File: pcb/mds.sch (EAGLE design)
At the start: 51 parts, among them IC1 MAX1555, Q1 CSTCR6M00G53Z, U2 ISD1900ISD1932, U5 ATMEGA328

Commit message: Code
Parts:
- R6: value (none) -> 56k
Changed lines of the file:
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@@
 <part name="SP-" library="wirepad" deviceset="2,15/1,0" device=""/>
 <part name="R8" library="rcl" deviceset="R-EU_" device="M0805" value="10k"/>
-<part name="R6" library="rcl" deviceset="R-EU_" device="M0805"/>
+<part name="R6" library="rcl" deviceset="R-EU_" device="M0805" value="56k"/>
 <part name="GND2" library="SparkFun" deviceset="GND" device=""/>
 <part name="R3" library="rcl" deviceset="R-EU_" device="M0805" value="4.7k"/>

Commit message: Code !
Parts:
- removed BTN: Button, SparkFun:TAC_SWITCHSMD
- removed MOT+, MOT-: (no value), wirepad:2,15/1,0
- removed RESET: Reset, SparkFun:TAC_SWITCHSMD
- added ADC1, VIB+, VIB-: (no value), wirepad:1,6/0,8
- added C13: 100nf, rcl:C-EUC0805
- added R9: 4.7k, rcl:R-EU_M0805
- added RST+, RST-: WIREPAD1,6/0,8, wirepad:WIREPAD1,6/0,8
- ADC0, LIPO+, LIPO-, MIC+, MIC-, PWR+, PWR-, SP+, SP-: device wirepad:2,15/1,0 -> wirepad:1,6/0,8
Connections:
- new net ADC1: ADC1.P, C13.1, U5.ADC7
- net ADC0: now also U5.ADC6; no longer BTN.1, BTN.2, U5.PC0(ADC0)
- net CHG: now also R9.1
- net GND: now also C13.2, RST-.P; no longer BTN.3, BTN.4, RESET.1, RESET.2
- net M3: now also U5.PC0(ADC0); no longer U5.ADC6
- net M4: no longer U5.ADC7
- net N$7: now also VIB-.P; no longer MOT-.P
- net RST: now also RST+.P; no longer RESET.3, RESET.4
- net VCC: now also R9.2, VIB+.P; no longer MOT+.P
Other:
- moved on the sheet: C10, C18

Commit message: Code + Cad
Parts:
- removed Q1: CSTCR6M00G53Z, murata-filter:CSTCR6M00G53Z
- added C14, C21, C22: 100nf, rcl:C-EUC0805
- added LED1: (no value), led:LEDCHIP-LED0805
- added R10: 4.7k, rcl:R-EU_M0805
- added U3: SF-BLUEGIGA_BLE112-A-VISUAL, ble112:SF-BLUEGIGA_BLE112-A-VISUAL
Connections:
- removed net N$9: Q1.3, U5.PB7(XTAL2/TOSC2)
- new net ??: U5.PB7(XTAL2/TOSC2)
- new net LEDB: R10.2, U3.P0_0
- new net RX: U3.P0_5
- new net TX: U3.P0_4
- net GND: now also C14.1, C21.1, C22.1, LED1.C, U3.GND, U3.GND@2, U3.GND@3, U3.GND@4; no longer Q1.2
- net M4: now also U5.PC1(ADC1)
- net N$10: now also LED1.A, R10.1; no longer Q1.1, U5.PB6(XTAL1/TOSC1)
- net VCC: now also C14.2, C21.2, C22.2, U3.AVDD, U3.AVDD@2, U3.DVDD, U3.VDD_USB
- net VIBRATOR: now also U5.PB6(XTAL1/TOSC1); no longer U5.PC1(ADC1)
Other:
- note added: "Bluetooth"
- moved on the sheet: C1, C19, C2, C20, C3, C4, C5, C6, C7, C8, MIC+, MIC-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

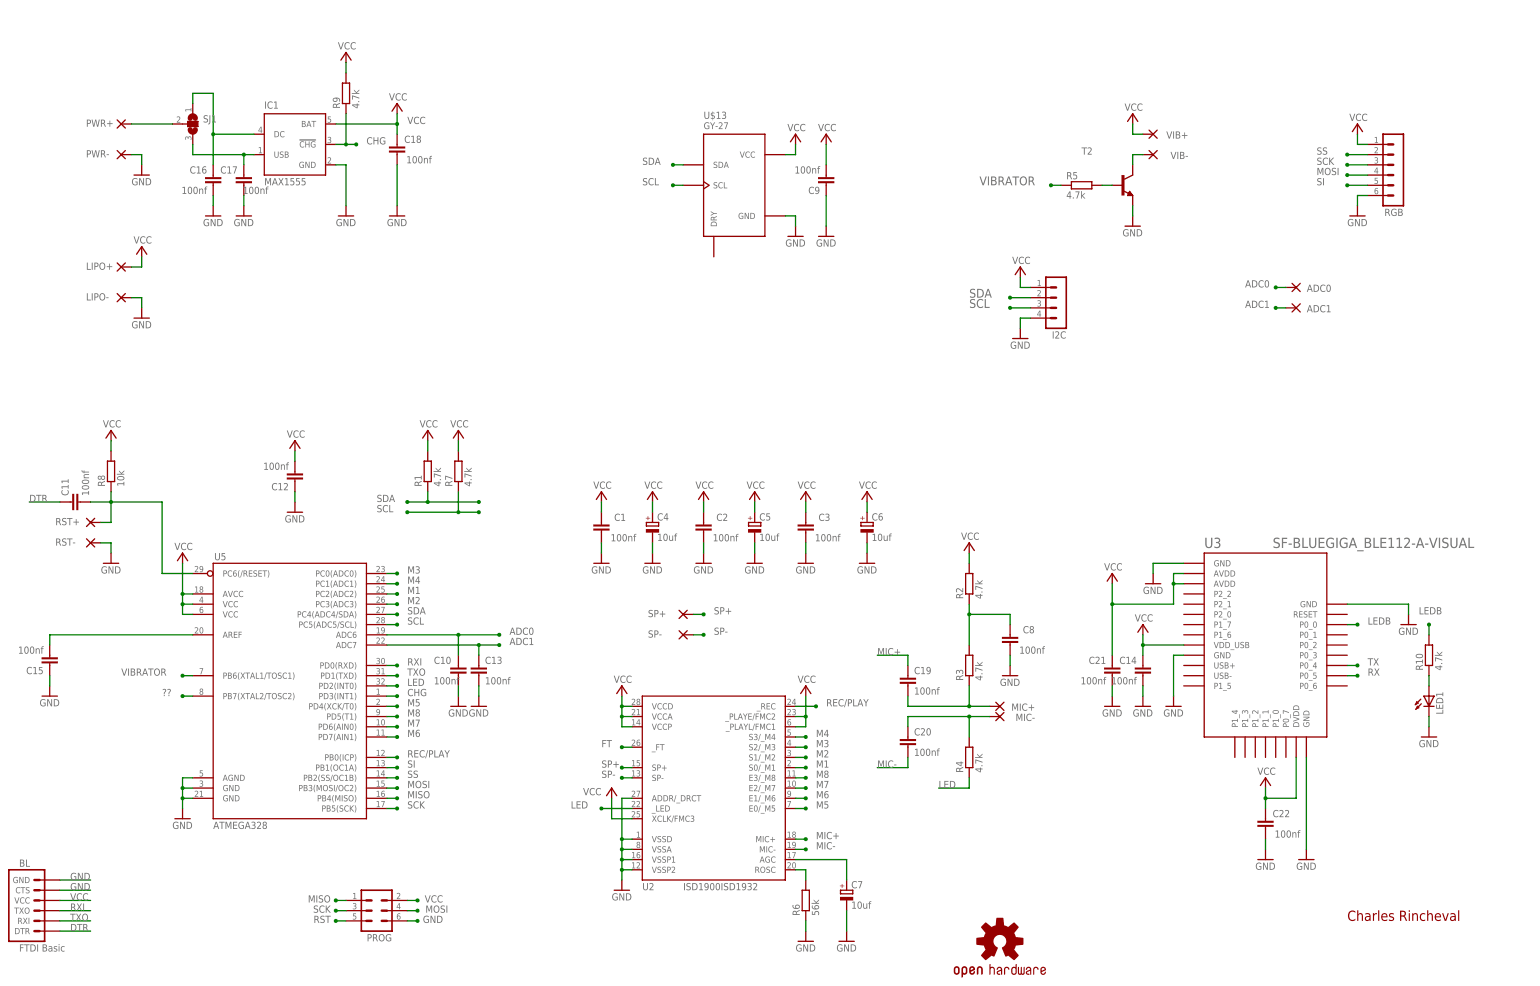
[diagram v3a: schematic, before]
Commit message: PCB : Bluetooth module + enhancement
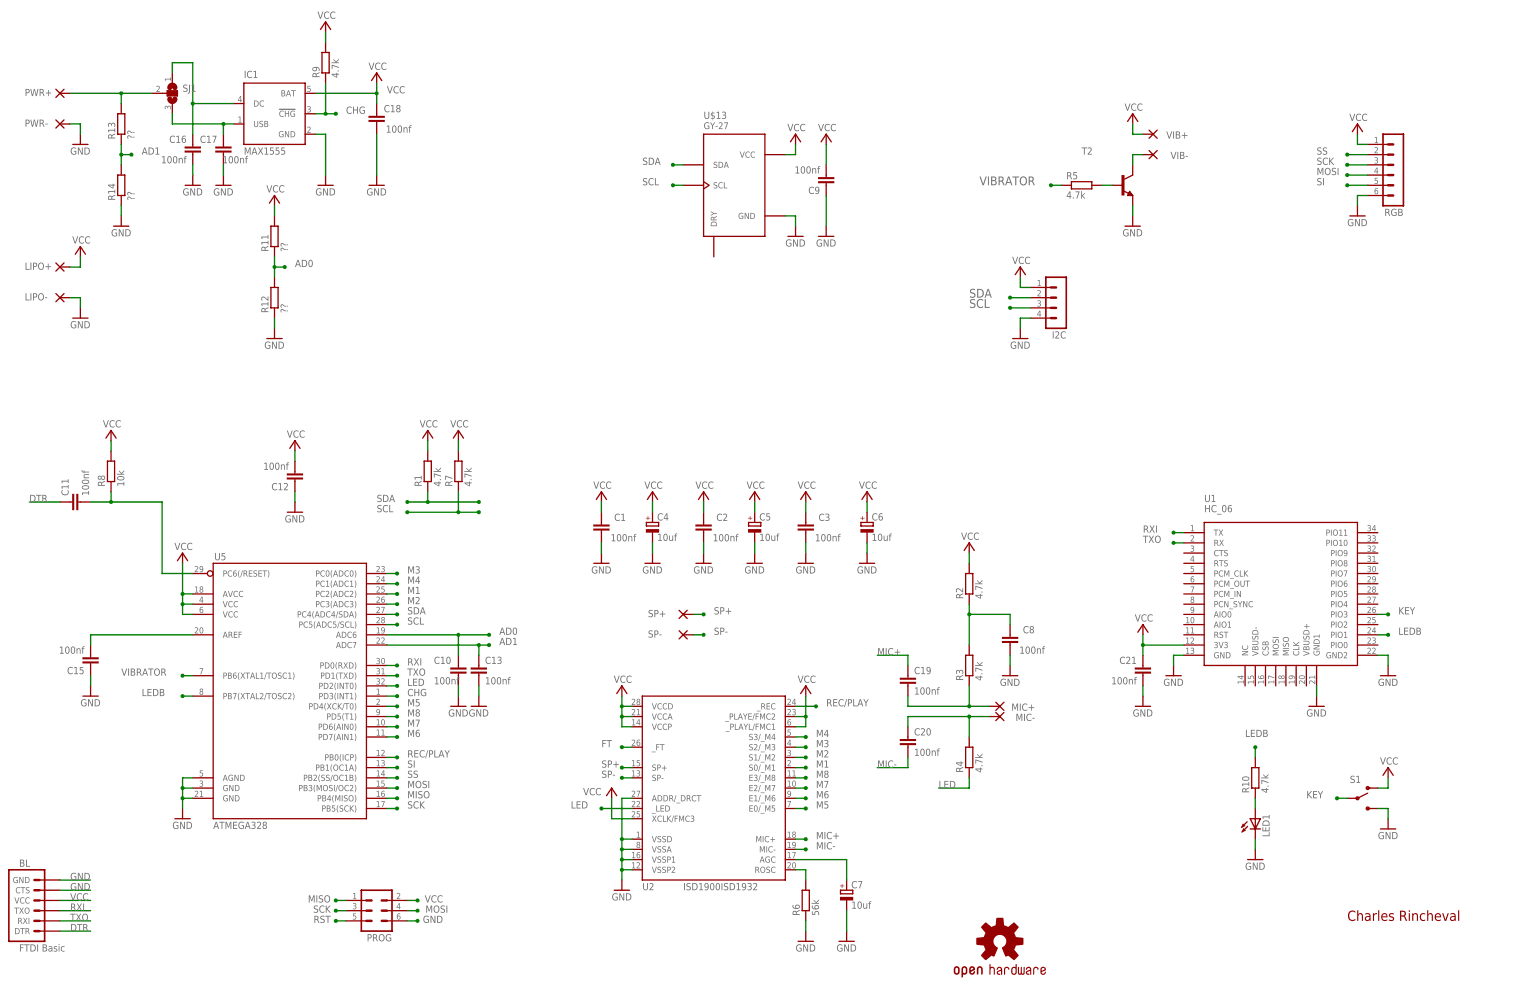
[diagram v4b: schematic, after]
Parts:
- removed ADC0, ADC1: (no value), wirepad:1,6/0,8
- removed C14, C22: 100nf, rcl:C-EUC0805
- removed RST+, RST-: WIREPAD1,6/0,8, wirepad:WIREPAD1,6/0,8
- removed U3: SF-BLUEGIGA_BLE112-A-VISUAL, ble112:SF-BLUEGIGA_BLE112-A-VISUAL
- added R11, R12, R13, R14: ??, rcl:R-EU_M0805
- added S1: (no value), SparkFun-Electromechanical:SWITCH-SPDTSMD2
- added U1: HC_06, Bluetooth HC-05:HC_05
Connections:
- removed net ??: U5.PB7(XTAL2/TOSC2)
- removed net ADC0: ADC0.P, C10.1, U5.ADC6
- removed net ADC1: ADC1.P, C13.1, U5.ADC7
- removed net RX: U3.P0_5
- removed net TX: U3.P0_4
- new net AD0: C10.1, R11.1, R12.2, U5.ADC6
- new net AD1: C13.1, R13.1, R14.2, U5.ADC7
- new net KEY: S1.P, U1.PIO3
- net GND: now also R12.1, R14.1, S1.S, U1.GND, U1.GND1, U1.GND2; no longer C14.1, C22.1, RST-.P, U3.GND, U3.GND@2, U3.GND@3, U3.GND@4
- net LEDB: now also U1.PIO1, U5.PB7(XTAL2/TOSC2); no longer U3.P0_0
- net N$8: now also R13.2
- net RST: no longer RST+.P
- net RXI: now also U1.TX
- net TXO: now also U1.RX
- net VCC: now also R11.2, S1.O, U1.3V3; no longer C14.2, C22.2, U3.AVDD, U3.AVDD@2, U3.DVDD, U3.VDD_USB
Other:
- moved on the sheet: C15, C16, C17, C18, C21, IC1, LED1, LIPO+, LIPO-, PWR+, PWR-, R10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

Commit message: PCB 0.8.0
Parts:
- removed LED1: (no value), led:LEDCHIP-LED0805
- added LED: (no value), led:LEDCHIP-LED0805
- added SJ2, SJ3: (no value), jumper:SJ2W
- BLUETOOTH: value HC_06 -> HC_0x
- renumbered U1 to BLUETOOTH
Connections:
- removed net KEY: BLUETOOTH.PIO3, S1.P
- new net HC05_KEY: BLUETOOTH.PIO11, SJ2.3
- new net HC05_LED: BLUETOOTH.PIO9, SJ3.3
- new net HC06_KEY: BLUETOOTH.PIO3, SJ2.1
- new net HC06_LED: BLUETOOTH.PIO1, SJ3.1
- new net N$4: S1.P, SJ2.2
- net GND: now also LED.C; no longer LED1.C
- net LEDB: now also SJ3.2; no longer BLUETOOTH.PIO1
- net N$10: now also LED.A; no longer LED1.A
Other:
- moved on the sheet: R10, S1
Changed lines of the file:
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@@
 <part name="C21" library="rcl" deviceset="C-EU" device="C0805" value="100nf"/>
 <part name="R10" library="rcl" deviceset="R-EU_" device="M0805" value="4.7k"/>
-<part name="LED1" library="led" deviceset="LED" device="CHIP-LED0805"/>
+<part name="LED" library="led" deviceset="LED" device="CHIP-LED0805"/>
 <part name="GND35" library="SparkFun" deviceset="GND" device=""/>
-<part name="U1" library="Bluetooth HC-05" deviceset="HC_05" device="" value="HC_06"/>
+<part name="BLUETOOTH" library="Bluetooth HC-05" deviceset="HC_05" device="" value="HC_0x"/>
 <part name="GND30" library="SparkFun" deviceset="GND" device=""/>
 <part name="GND31" library="SparkFun" deviceset="GND" device=""/>
@@
 <part name="R14" library="rcl" deviceset="R-EU_" device="M0805" value="??"/>
 <part name="GND33" library="SparkFun" deviceset="GND" device=""/>
+<part name="SJ2" library="jumper" deviceset="SJ2W" device=""/>
+<part name="SJ3" library="jumper" deviceset="SJ2W" device=""/>
 </parts>
 <sheets>
@@
 <attribute name="VALUE" x="295.656" y="80.899" size="1.778" layer="96" rot="R180"/>
 </instance>
-<instance part="R10" gate="G$1" x="325.12" y="55.88" rot="R90"/>
-<instance part="LED1" gate="G$1" x="325.12" y="45.72"/>
-<instance part="GND35" gate="1" x="325.12" y="35.56"/>
-<instance part="U1" gate="G$1" x="330.2" y="101.6"/>
+<instance part="R10" gate="G$1" x="297.18" y="55.88" rot="R90"/>
+<instance part="LED" gate="G$1" x="297.18" y="45.72"/>
+<instance part="GND35" gate="1" x="297.18" y="35.56"/>
+<instance part="BLUETOOTH" gate="G$1" x="330.2" y="101.6"/>
 <instance part="GND30" gate="1" x="304.8" y="81.28"/>
 <instance part="GND31" gate="1" x="340.36" y="73.66"/>
-<instance part="S1" gate="1" x="350.52" y="50.8" smashed="yes">
-<attribute name="NAME" x="348.615" y="54.61" size="1.778" layer="95"/>
-<attribute name="VALUE" x="347.98" y="54.61" size="1.778" layer="96"/>
-</instance>
-<instance part="GND27" gate="1" x="358.14" y="43.18"/>
-<instance part="P+25" gate="VCC" x="358.14" y="58.42" smashed="yes">
-<attribute name="VALUE" x="360.68" y="60.96" size="1.778" layer="96" rot="R180"/>
+<instance part="S1" gate="1" x="330.2" y="50.8" smashed="yes">
+<attribute name="NAME" x="328.295" y="54.61" size="1.778" layer="95"/>
+<attribute name="VALUE" x="327.66" y="54.61" size="1.778" layer="96"/>
+</instance>
+<instance part="GND27" gate="1" x="337.82" y="43.18"/>
+<instance part="P+25" gate="VCC" x="337.82" y="58.42" smashed="yes">
+<attribute name="VALUE" x="340.36" y="60.96" size="1.778" layer="96" rot="R180"/>
 </instance>
 <instance part="GND32" gate="1" x="358.14" y="81.28"/>
@@
 <instance part="R14" gate="G$1" x="43.18" y="203.2" rot="R90"/>
 <instance part="GND33" gate="1" x="43.18" y="193.04"/>
+<instance part="SJ2" gate="G$1" x="320.04" y="50.8" rot="R180"/>
+<instance part="SJ3" gate="G$1" x="358.14" y="50.8" rot="R180"/>
 </instances>
 <busses>
@@
 </segment>
 <segment>
-<pinref part="LED1" gate="G$1" pin="C"/>
+<pinref part="LED" gate="G$1" pin="C"/>
 <pinref part="GND35" gate="1" pin="GND"/>
-<wire x1="325.12" y1="40.64" x2="325.12" y2="38.1" width="0.1524" layer="91"/>
-</segment>
-<segment>
-<pinref part="U1" gate="G$1" pin="GND"/>
+<wire x1="297.18" y1="40.64" x2="297.18" y2="38.1" width="0.1524" layer="91"/>
+</segment>
+<segment>
+<pinref part="BLUETOOTH" gate="G$1" pin="GND"/>
 <wire x1="307.34" y1="86.36" x2="304.8" y2="86.36" width="0.1524" layer="91"/>
 <wire x1="304.8" y1="86.36" x2="304.8" y2="83.82" width="0.1524" layer="91"/>
@@
 </segment>
 <segment>
-<pinref part="U1" gate="G$1" pin="GND1"/>
+<pinref part="BLUETOOTH" gate="G$1" pin="GND1"/>
 <wire x1="340.36" y1="78.74" x2="340.36" y2="76.2" width="0.1524" layer="91"/>
 <pinref part="GND31" gate="1" pin="GND"/>
@@
 <segment>
 <pinref part="S1" gate="1" pin="S"/>
-<wire x1="355.6" y1="48.26" x2="358.14" y2="48.26" width="0.1524" layer="91"/>
+<wire x1="335.28" y1="48.26" x2="337.82" y2="48.26" width="0.1524" layer="91"/>
 <pinref part="GND27" gate="1" pin="GND"/>
-<wire x1="358.14" y1="48.26" x2="358.14" y2="45.72" width="0.1524" layer="91"/>
-</segment>
-<segment>
-<pinref part="U1" gate="G$1" pin="GND2"/>
+<wire x1="337.82" y1="48.26" x2="337.82" y2="45.72" width="0.1524" layer="91"/>
+</segment>
+<segment>
+<pinref part="BLUETOOTH" gate="G$1" pin="GND2"/>
 <wire x1="355.6" y1="86.36" x2="358.14" y2="86.36" width="0.1524" layer="91"/>
 <pinref part="GND32" gate="1" pin="GND"/>
@@
 </segment>
 <segment>
-<pinref part="U1" gate="G$1" pin="3V3"/>
+<pinref part="BLUETOOTH" gate="G$1" pin="3V3"/>
 <wire x1="307.34" y1="88.9" x2="297.18" y2="88.9" width="0.1524" layer="91"/>
 <wire x1="297.18" y1="88.9" x2="297.18" y2="91.44" width="0.1524" layer="91"/>
@@
 <segment>
 <pinref part="S1" gate="1" pin="O"/>
-<wire x1="355.6" y1="53.34" x2="358.14" y2="53.34" width="0.1524" layer="91"/>
+<wire x1="335.28" y1="53.34" x2="337.82" y2="53.34" width="0.1524" layer="91"/>
 <pinref part="P+25" gate="VCC" pin="VCC"/>
-<wire x1="358.14" y1="53.34" x2="358.14" y2="55.88" width="0.1524" layer="91"/>
+<wire x1="337.82" y1="53.34" x2="337.82" y2="55.88" width="0.1524" layer="91"/>
 </segment>
 <segment>
@@
 </segment>
 <segment>
-<pinref part="U1" gate="G$1" pin="RX"/>
+<pinref part="BLUETOOTH" gate="G$1" pin="RX"/>
 <wire x1="307.34" y1="114.3" x2="304.8" y2="114.3" width="0.1524" layer="91"/>
 <junction x="304.8" y="114.3"/>
@@
 </segment>
 <segment>
-<pinref part="U1" gate="G$1" pin="TX"/>
+<pinref part="BLUETOOTH" gate="G$1" pin="TX"/>
 <wire x1="307.34" y1="116.84" x2="304.8" y2="116.84" width="0.1524" layer="91"/>
 <junction x="304.8" y="116.84"/>
@@
 <segment>
 <pinref part="R10" gate="G$1" pin="1"/>
-<pinref part="LED1" gate="G$1" pin="A"/>
-<wire x1="325.12" y1="48.26" x2="325.12" y2="50.8" width="0.1524" layer="91"/>
+<pinref part="LED" gate="G$1" pin="A"/>
+<wire x1="297.18" y1="48.26" x2="297.18" y2="50.8" width="0.1524" layer="91"/>
 </segment>
 </net>
 <net name="LEDB" class="0">
 <segment>
-<pinref part="U1" gate="G$1" pin="PIO1"/>
-<wire x1="355.6" y1="91.44" x2="358.14" y2="91.44" width="0.1524" layer="91"/>
-<junction x="358.14" y="91.44"/>
-<label x="360.68" y="91.44" size="1.778" layer="95"/>
-</segment>
-<segment>
 <pinref part="R10" gate="G$1" pin="2"/>
-<wire x1="325.12" y1="60.96" x2="325.12" y2="63.5" width="0.1524" layer="91"/>
-<junction x="325.12" y="63.5"/>
-<label x="322.58" y="66.04" size="1.778" layer="95"/>
+<wire x1="297.18" y1="60.96" x2="297.18" y2="63.5" width="0.1524" layer="91"/>
+<junction x="297.18" y="63.5"/>
+<label x="294.64" y="66.04" size="1.778" layer="95"/>
 </segment>
 <segment>
@@
 <label x="48.26" y="76.2" size="1.778" layer="95"/>
 </segment>
-</net>
-<net name="KEY" class="0">
-<segment>
-<pinref part="U1" gate="G$1" pin="PIO3"/>
+<segment>
+<pinref part="SJ3" gate="G$1" pin="2"/>
+<wire x1="363.22" y1="50.8" x2="365.76" y2="50.8" width="0.1524" layer="91"/>
+<junction x="365.76" y="50.8"/>
+<label x="368.3" y="50.8" size="1.778" layer="95"/>
+</segment>
+</net>
+<net name="HC06_KEY" class="0">
+<segment>
+<pinref part="BLUETOOTH" gate="G$1" pin="PIO3"/>
 <wire x1="355.6" y1="96.52" x2="358.14" y2="96.52" width="0.1524" layer="91"/>
 <junction x="358.14" y="96.52"/>
@@
 </segment>
 <segment>
-<pinref part="S1" gate="1" pin="P"/>
-<wire x1="347.98" y1="50.8" x2="345.44" y2="50.8" width="0.1524" layer="91"/>
-<junction x="345.44" y="50.8"/>
-<label x="337.82" y="50.8" size="1.778" layer="95"/>
+<pinref part="SJ2" gate="G$1" pin="1"/>
+<wire x1="320.04" y1="45.72" x2="320.04" y2="43.18" width="0.1524" layer="91"/>
+<junction x="320.04" y="43.18"/>
+<label x="314.96" y="38.1" size="1.778" layer="95"/>
 </segment>
 </net>
@@
 </segment>
 </net>
+<net name="N$4" class="0">
+<segment>
+<pinref part="S1" gate="1" pin="P"/>
+<pinref part="SJ2" gate="G$1" pin="2"/>
+<wire x1="325.12" y1="50.8" x2="327.66" y2="50.8" width="0.1524" layer="91"/>
+</segment>
+</net>
+<net name="HC05_KEY" class="0">
+<segment>
+<pinref part="SJ2" gate="G$1" pin="3"/>
+<wire x1="320.04" y1="55.88" x2="320.04" y2="58.42" width="0.1524" layer="91"/>
+<junction x="320.04" y="58.42"/>
+<label x="314.96" y="60.96" size="1.778" layer="95"/>
+</segment>
+<segment>
+<pinref part="BLUETOOTH" gate="G$1" pin="PIO11"/>
+<wire x1="355.6" y1="116.84" x2="358.14" y2="116.84" width="0.1524" layer="91"/>
+<junction x="358.14" y="116.84"/>
+<label x="360.68" y="116.84" size="1.778" layer="95"/>
+</segment>
+</net>
+<net name="HC05_LED" class="0">
+<segment>
+<pinref part="BLUETOOTH" gate="G$1" pin="PIO9"/>
+<wire x1="355.6" y1="111.76" x2="358.14" y2="111.76" width="0.1524" layer="91"/>
+<junction x="358.14" y="111.76"/>
+<label x="360.68" y="111.76" size="1.778" layer="95"/>
+</segment>
+<segment>
+<pinref part="SJ3" gate="G$1" pin="3"/>
+<wire x1="358.14" y1="55.88" x2="358.14" y2="58.42" width="0.1524" layer="91"/>
+<junction x="358.14" y="58.42"/>
+<label x="353.06" y="60.96" size="1.778" layer="95"/>
+</segment>
+</net>
+<net name="HC06_LED" class="0">
+<segment>
+<pinref part="SJ3" gate="G$1" pin="1"/>
+<wire x1="358.14" y1="45.72" x2="358.14" y2="43.18" width="0.1524" layer="91"/>
+<junction x="358.14" y="43.18"/>
+<label x="353.06" y="38.1" size="1.778" layer="95"/>
+</segment>
+<segment>
+<pinref part="BLUETOOTH" gate="G$1" pin="PIO1"/>
+<wire x1="355.6" y1="91.44" x2="358.14" y2="91.44" width="0.1524" layer="91"/>
+<junction x="358.14" y="91.44"/>
+<label x="360.68" y="91.44" size="1.778" layer="95"/>
+</segment>
+</net>

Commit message: Clean, code, openscad
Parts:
- R11: value ?? -> 6.8k 1%
- R12: value ?? -> 2.2k 1%
- R13: value ?? -> 10k
- R14: value ?? -> 1k5
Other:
- note added: "LIPO Max : 4.5V"
- note added: "PWR Max : 7V"
- note added: "R11 & R12 calculated for AD0 = 1.1V when LIPO = 4.5V"
- note added: "R13 & R14 value calculated for AD1 ~ 1.1V when PWR = 7V"
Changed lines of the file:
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@@
 <part name="P+25" library="supply1" deviceset="VCC" device=""/>
 <part name="GND32" library="SparkFun" deviceset="GND" device=""/>
-<part name="R11" library="rcl" deviceset="R-EU_" device="M0805" value="??"/>
-<part name="R12" library="rcl" deviceset="R-EU_" device="M0805" value="??"/>
+<part name="R11" library="rcl" deviceset="R-EU_" device="M0805" value="6.8k 1%"/>
+<part name="R12" library="rcl" deviceset="R-EU_" device="M0805" value="2.2k 1%"/>
 <part name="GND14" library="SparkFun" deviceset="GND" device=""/>
 <part name="P+27" library="supply1" deviceset="VCC" device=""/>
-<part name="R13" library="rcl" deviceset="R-EU_" device="M0805" value="??"/>
-<part name="R14" library="rcl" deviceset="R-EU_" device="M0805" value="??"/>
+<part name="R13" library="rcl" deviceset="R-EU_" device="M0805" value="10k"/>
+<part name="R14" library="rcl" deviceset="R-EU_" device="M0805" value="1k5"/>
 <part name="GND33" library="SparkFun" deviceset="GND" device=""/>
 <part name="SJ2" library="jumper" deviceset="SJ2W" device=""/>
@@
 <wire x1="279.4" y1="154.94" x2="279.4" y2="5.08" width="0.1524" layer="98" style="shortdash"/>
 <text x="287.02" y="142.24" size="6.4516" layer="98">Bluetooth</text>
+<text x="35.56" y="177.8" size="1.778" layer="98">LIPO Max : 4.5V</text>
+<text x="10.16" y="231.14" size="1.778" layer="98">PWR Max : 7V</text>
+<wire x1="40.64" y1="213.36" x2="35.56" y2="218.44" width="0.1524" layer="98"/>
+<wire x1="35.56" y1="218.44" x2="35.56" y2="231.14" width="0.1524" layer="98"/>
+<wire x1="35.56" y1="231.14" x2="48.26" y2="243.84" width="0.1524" layer="98"/>
+<text x="48.26" y="246.38" size="1.778" layer="98">R13 &amp; R14 value calculated for
+AD1 ~ 1.1V when PWR = 7V</text>
+<text x="96.52" y="190.5" size="1.778" layer="98">R11 &amp; R12 calculated for AD0 = 1.1V
+when LIPO = 4.5V</text>
+<wire x1="93.98" y1="193.04" x2="91.44" y2="193.04" width="0.1524" layer="98"/>
+<wire x1="91.44" y1="193.04" x2="86.36" y2="187.96" width="0.1524" layer="98"/>
 </plain>
 <instances>
@@
 </schematic>
 </drawing>
+<compatibility>
+<note version="6.3" minversion="6.2.2" severity="warning">
+Since Version 6.2.2 text objects can contain more than one line,
+which will not be processed correctly with this version.
+</note>
+</compatibility>
 </eagle>
